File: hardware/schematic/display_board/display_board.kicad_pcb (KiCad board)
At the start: 2 copper layers, 62 x 58.5 mm, 7 parts, among them J1 Conn_01x04_Pin, SW1 SW_Push, SW2 SW_Push

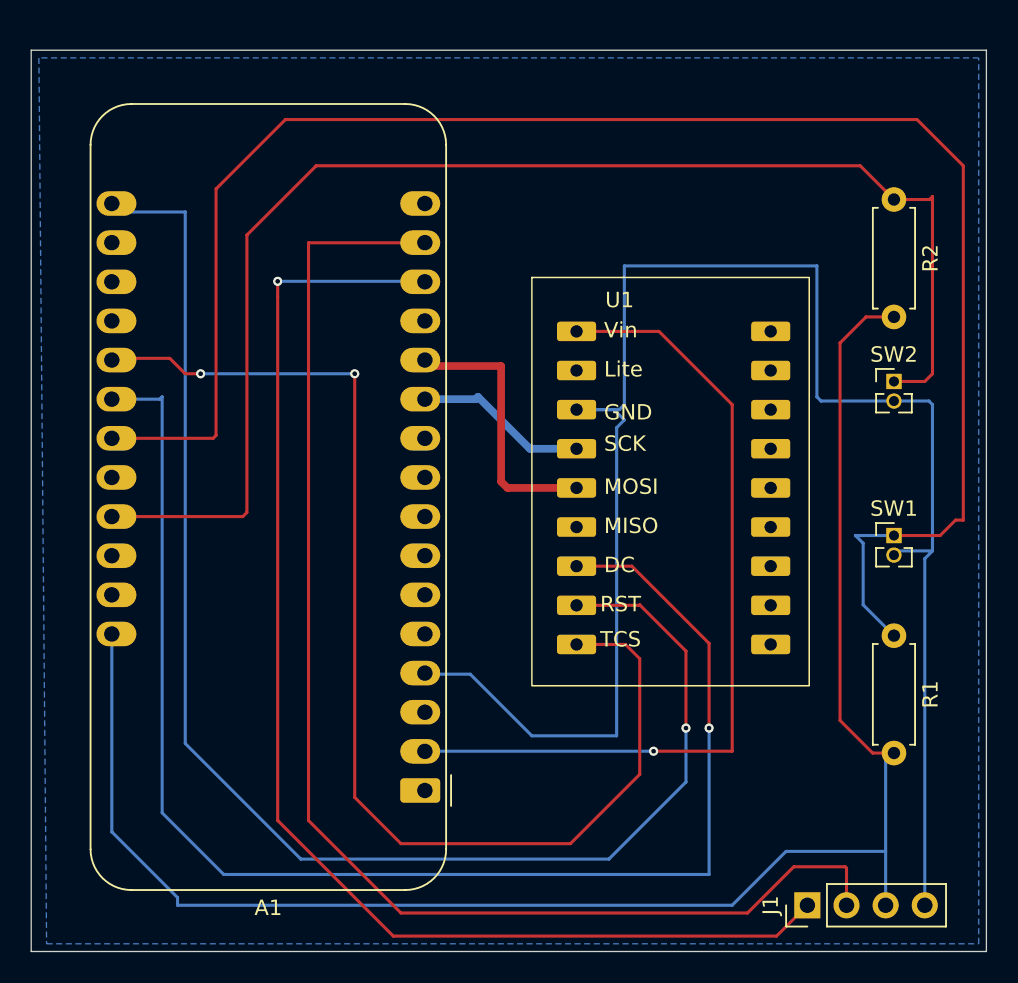
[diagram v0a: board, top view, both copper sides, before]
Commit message: updating pcb
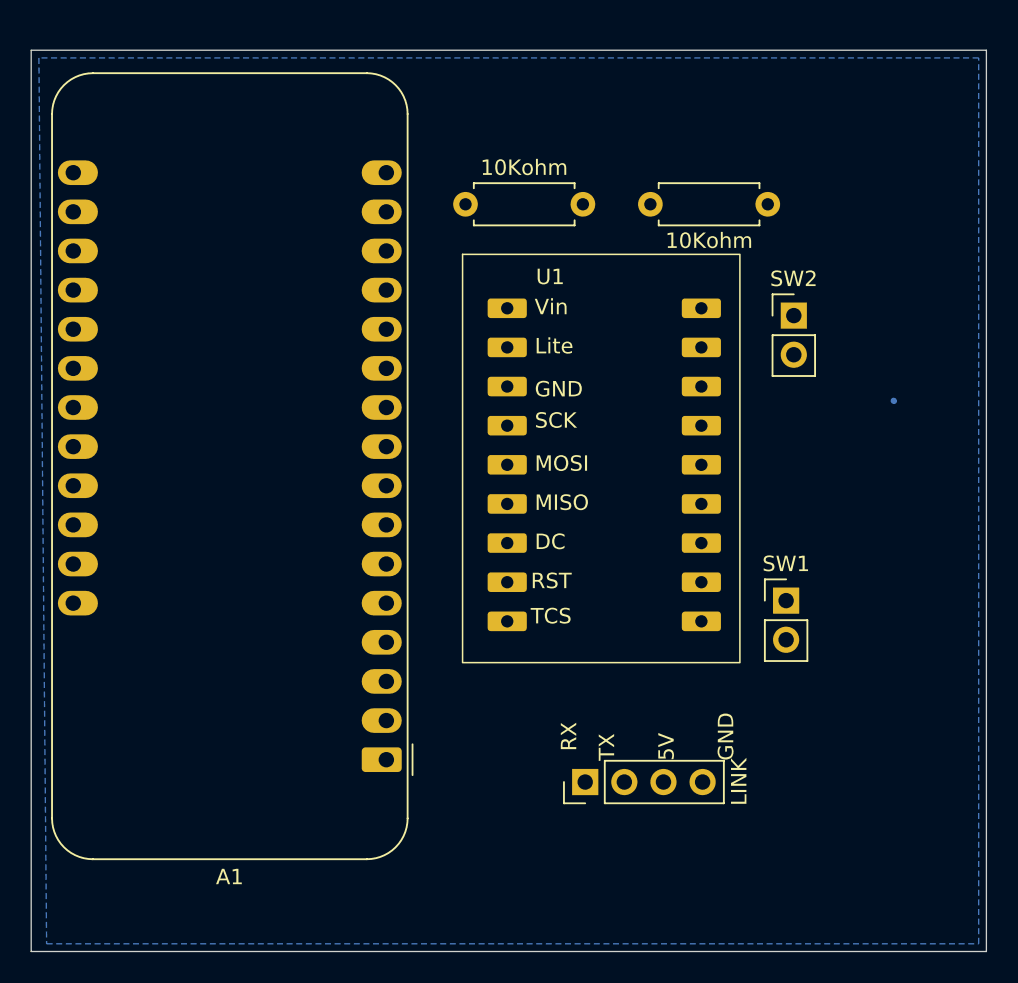
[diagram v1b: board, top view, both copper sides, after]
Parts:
- J1: value Conn_01x04_Pin -> LINK
- SW1, SW2: footprint Connector_PinHeader_1.27mm:PinHeader_1x02_P1.27mm_Vertical -> Connector_PinHeader_2.54mm:PinHeader_1x02_P2.54mm_Vertical
- moved 10Kohm 29.2 mm to (133.8, 77.0), turned to 180 degrees
- moved 10Kohm 27.8 mm to (114.2, 77.0), turned to 0 degrees
- moved J1 16.5 mm to (122.0, 114.5)
- moved SW1 8.18 mm to (135.0, 102.7)
- moved SW2 7.78 mm to (135.5, 84.2)
- moved U1 4.74 mm to (116.9, 83.8)
- moved A1 3.20 mm to (109.1, 113.0)
- renumbered R2 to 10Kohm, R1 to 10Kohm
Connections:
- net Net-(A1-3V3) renamed /3V3
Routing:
- net GND: track 114.5 -> 0.03 mm
- net Net-(A1-A10/IO27): track 112.4 -> 0.00 mm
- net +5V: track 110.1 -> 0.00 mm
- net Net-(A1-SDA/IO23): track 94.0 -> 0.00 mm, vias 1 -> 0
- net Net-(A1-A9/IO33): track 93.2 -> 0.00 mm, vias 1 -> 0
- net Net-(A1-A12/IO13): track 88.4 -> 0.00 mm
- net Net-(A1-TX/IO17): track 86.2 -> 0.00 mm
- net Net-(A1-RX/IO16): track 82.9 -> 0.00 mm, vias 1 -> 0
- net Net-(A1-A8/IO15): track 77.3 -> 0.00 mm, vias 2 -> 0
- net /3V3: track 54.4 -> 0.00 mm, vias 1 -> 0
- net Net-(A1-MOSI/IO18): track 17.7 -> 0.00 mm
- net Net-(A1-SCK/IO5): track 11.3 -> 0.00 mm
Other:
- board text added: "5V"
- board text added: "GND"
- board text added: "RX"
- board text added: "TX"

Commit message: First version of Nav PCB
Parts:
- J1: value LINK -> Conn_01x04_Pin; footprint Connector_PinHeader_2.54mm:PinHeader_1x04_P2.54mm_Vertical -> TerminalBlock:TerminalBlock_MaiXu_MX126-5.0-04P_1x04_P5.00mm
- SW1, SW2: footprint Connector_PinHeader_2.54mm:PinHeader_1x02_P2.54mm_Vertical -> TerminalBlock:TerminalBlock_MaiXu_MX126-5.0-02P_1x02_P5.00mm
- moved SW1 9.81 mm to (138.2, 93.5)
- moved J1 6.29 mm to (123.8, 108.5), turned to 0 degrees
- moved R1 6.00 mm to (133.6, 71.0)
- moved R2 6.00 mm to (114.2, 71.0)
- moved SW2 5.07 mm to (138.2, 80.0)
- moved U1 4.53 mm to (117.4, 79.2)
- moved A1 2.69 mm to (109.1, 110.4)
- renumbered 10Kohm to R1, 10Kohm to R2
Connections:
- net Net-(A1-A8/IO15) renamed /DC
- net Net-(A1-SCK/IO5) renamed /MOSI
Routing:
- net +5V: track 0.00 -> 112.3 mm
- net Net-(A1-A10/IO27): track 0.00 -> 90.7 mm
- net Net-(A1-A12/IO13): track 0.00 -> 88.1 mm, vias 0 -> 1
- net GND: track 0.03 -> 87.9 mm
- net Net-(A1-SDA/IO23): track 0.00 -> 84.5 mm, vias 0 -> 1
- net Net-(A1-A9/IO33): track 0.00 -> 70.3 mm, vias 0 -> 1
- net /DC: track 0.00 -> 69.7 mm
- net Net-(A1-TX/IO17): track 0.00 -> 49.2 mm
- net Net-(A1-RX/IO16): track 0.00 -> 44.2 mm
- net /3V3: track 0.00 -> 35.8 mm, vias 0 -> 2
- net Net-(A1-MOSI/IO18): track 0.00 -> 15.4 mm
- net /MOSI: track 0.00 -> 9.05 mm
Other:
- board size 62 x 58.5 mm -> 62 x 49 mm

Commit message: Collection of display improvements
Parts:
- J1: footprint TerminalBlock:TerminalBlock_MaiXu_MX126-5.0-04P_1x04_P5.00mm -> Connector_Molex:Molex_PicoBlade_53047-0410_1x04_P1.25mm_Vertical
- SW1, SW2: footprint TerminalBlock:TerminalBlock_MaiXu_MX126-5.0-02P_1x02_P5.00mm -> Connector_Molex:Molex_PicoBlade_53047-0210_1x02_P1.25mm_Vertical
- moved SW1 23.8 mm to (119.0, 79.5)
- moved U1 19.2 mm to (135.2, 86.4), turned to -90 degrees
- moved SW2 8.76 mm to (129.5, 79.5)
- moved J1 1.89 mm to (122.6, 107.0)
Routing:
- net +5V: track 112.3 -> 138.0 mm
- net Net-(A1-A12/IO13): track 88.1 -> 67.8 mm
- net Net-(A1-A10/IO27): track 90.7 -> 72.3 mm
- net Net-(A1-TX/IO17): track 49.2 -> 65.0 mm
- net GND: track 87.9 -> 72.3 mm
- net Net-(A1-A9/IO33): track 70.3 -> 83.0 mm, vias 1 -> 2
- net /MOSI: track 9.05 -> 21.1 mm
- net /DC: track 69.7 -> 81.7 mm, vias 0 -> 1
- net Net-(A1-RX/IO16): track 44.2 -> 55.2 mm
- net Net-(A1-SDA/IO23): track 84.5 -> 95.0 mm, vias 1 -> 2
- net /3V3: track 35.8 -> 45.9 mm, vias 2 -> 0
- net Net-(A1-MOSI/IO18): track 15.4 -> 19.3 mm
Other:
- board size 62 x 49 mm -> 54 x 49 mm

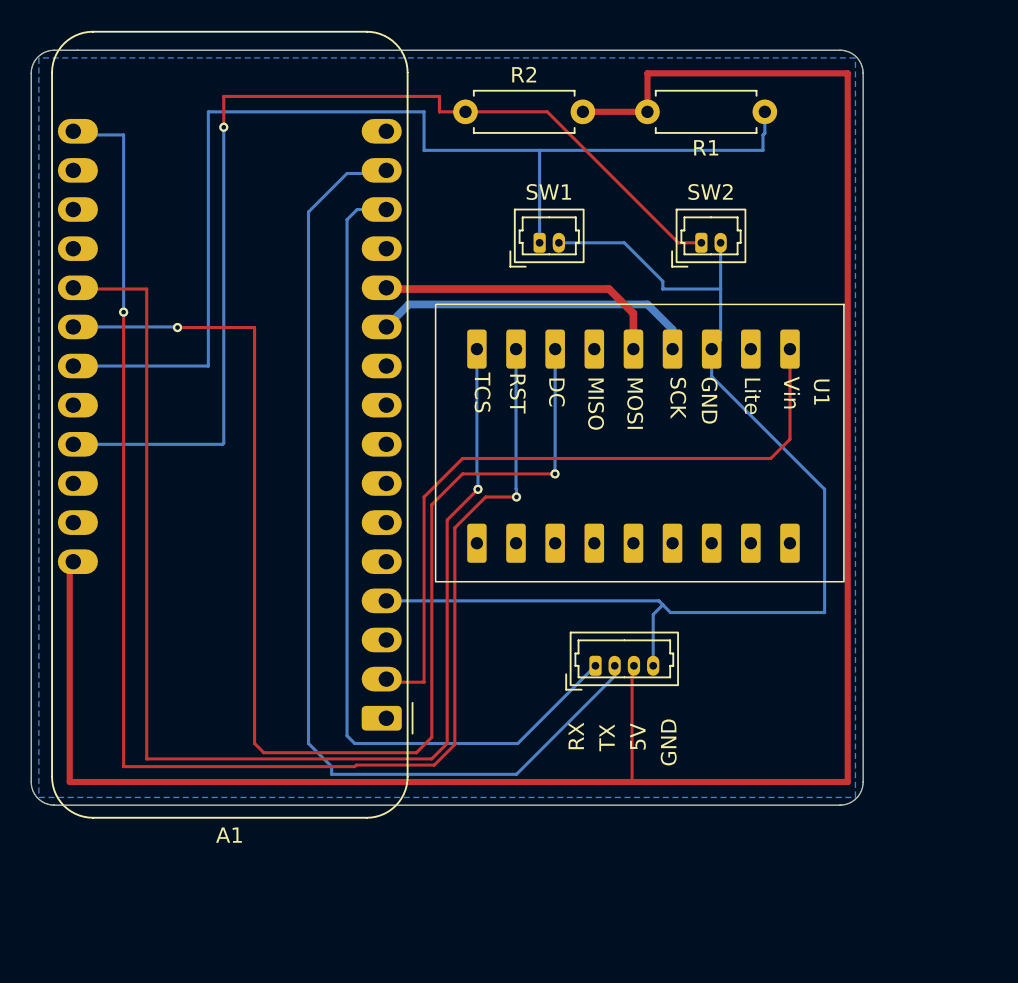
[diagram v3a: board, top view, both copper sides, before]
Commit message: Added improved wireless control - now it joins a known wireless station, which is helpful in the dive locker. Added two-button turn-on (and low power mode) Improved GPS performance with hot-start Reduced logging frequency; LOW should now be viable for long dives Updated display board
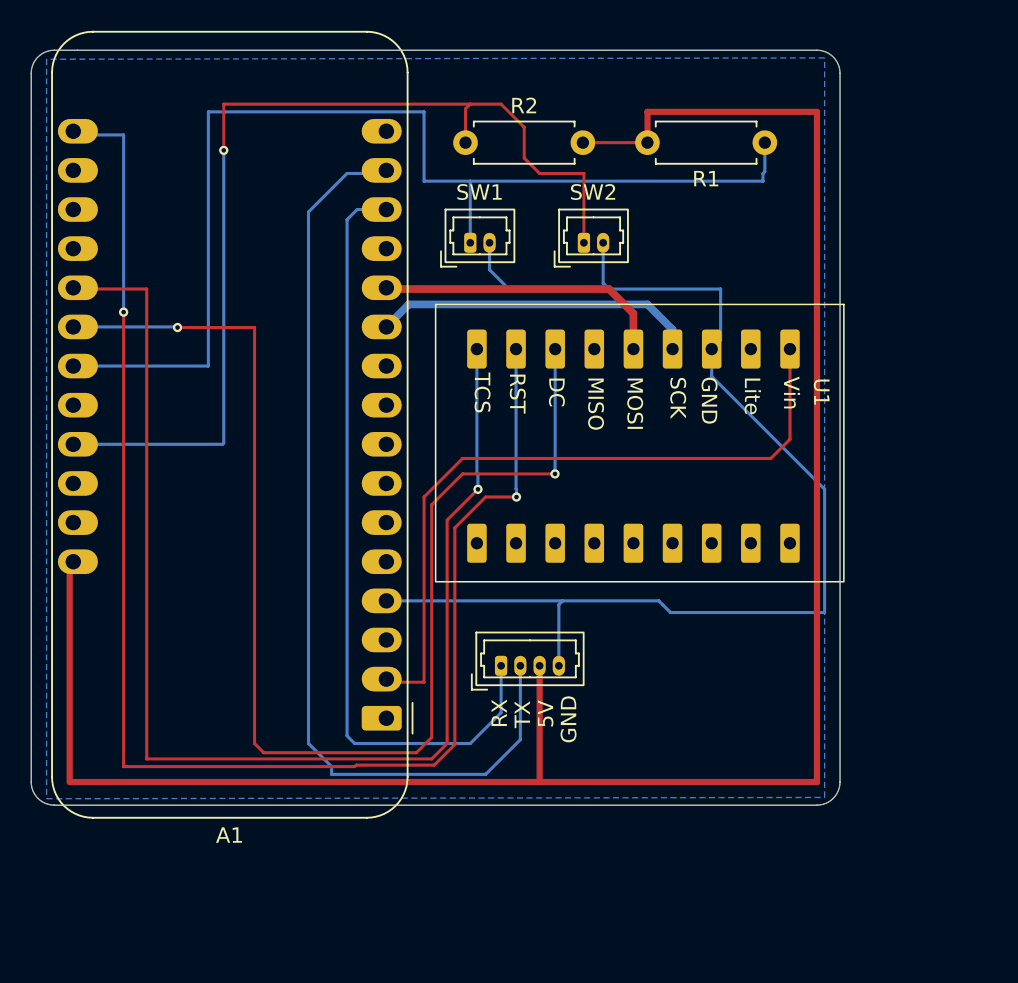
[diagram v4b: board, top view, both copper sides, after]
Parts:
- moved SW2 7.62 mm to (121.9, 79.5)
- moved J1 6.12 mm to (116.5, 107.0)
- moved SW1 4.50 mm to (114.5, 79.5)
- moved R1 2.00 mm to (133.6, 73.0)
- moved R2 2.00 mm to (114.2, 73.0)
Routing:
- net +5V: track 138.0 -> 130.9 mm
- net GND: track 72.3 -> 77.8 mm
- net Net-(A1-RX/IO16): track 55.2 -> 50.9 mm
- net Net-(A1-TX/IO17): track 65.0 -> 61.3 mm
- net Net-(A1-A12/IO13): track 67.8 -> 65.3 mm
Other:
- board size 54 x 49 mm -> 52.5 x 49 mm
